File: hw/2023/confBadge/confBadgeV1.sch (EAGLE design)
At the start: 51 parts, among them J1 10118192-0002LF, Q1 8/16/20MHz, U1 ATMEGA328, U10 WS2812-2020, U11 WS2812-2020, U12 WS2812-2020, U13 WS2812-2020, U14 WS2812-2020, U15 WS2812-2020, U16 WS2812-2020, U17 WS2812-2020, U18 WS2812-2020, U19 WS2812-2020, U2 AP2112-3.3, U20 WS2812-2020, U3 WS2812-2020, U4 WS2812-2020, U5 PCM12SMTRPCM12SMTR_CNK, U6 24792479PCB_37P49X52P63_KEY, U7 CH340C, U8 SMF05CT1G, U9 WS2812-2020

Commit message: Completed part placement
- parts placement done
-added cap to each neopixel
- connected usb power to regulator
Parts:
- added C10, C11, C12, C13, C14, C15, C16, C17, C18, C19, C4, C5, C6, C7, C8, C9: 0.1uF, SparkFun:CAP0603-CAP
- added D2: RED, microbuilder:LED0805_NOOUTLINE
- added U21, U22: WS2812-2020, WS2812-2020:WS2812-2020
- D3: value Green -> MBR120; device Testing:LED -> microbuilder:DIODE-SCHOTTKYSOD-123
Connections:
- removed net VCC: C3.2
- new net N$17: U20.DO, U21.DI
- new net N$20: U21.DO, U22.DI
- net 3.3V: now also C3.2
- net GND: now also C10.1, C11.1, C12.1, C13.1, C14.1, C15.1, C16.1, C17.1, C18.1, C19.1, C4.1, C5.1, C6.1, C7.1, C8.1, C9.1, D2.C, U21.GND, U22.GND; no longer D3.C
- net N$34: now also D3.C
- net N$7: now also D2.A; no longer D3.A
- net VBUS: now also D3.A
- net VDD: now also C10.2, C11.2, C12.2, C13.2, C14.2, C15.2, C16.2, C17.2, C18.2, C19.2, C4.2, C5.2, C6.2, C7.2, C8.2, C9.2, U21.VDD, U22.VDD
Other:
- moved on the sheet: U10, U11, U12, U13, U14, U15, U16, U17, U18, U19, U20, U3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

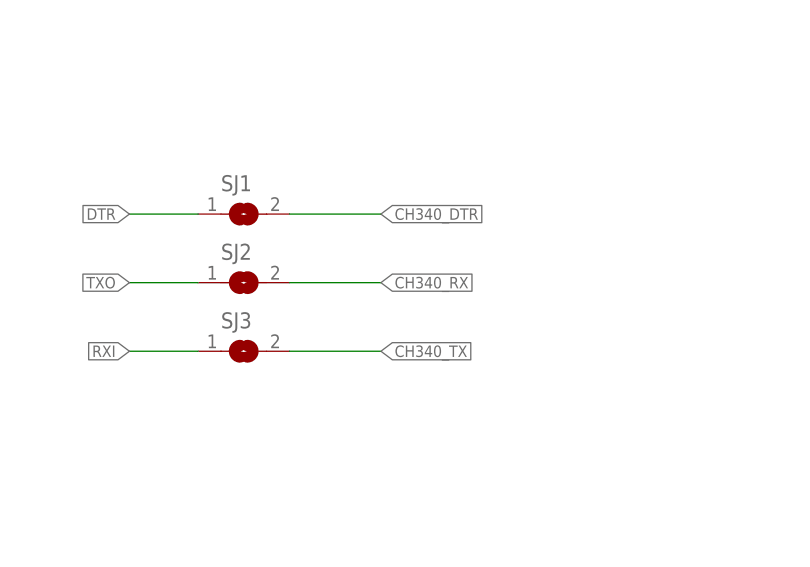
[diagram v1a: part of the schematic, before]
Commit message: Tested monochrome bitmap
Added Rao to the back of the confBadge for testing
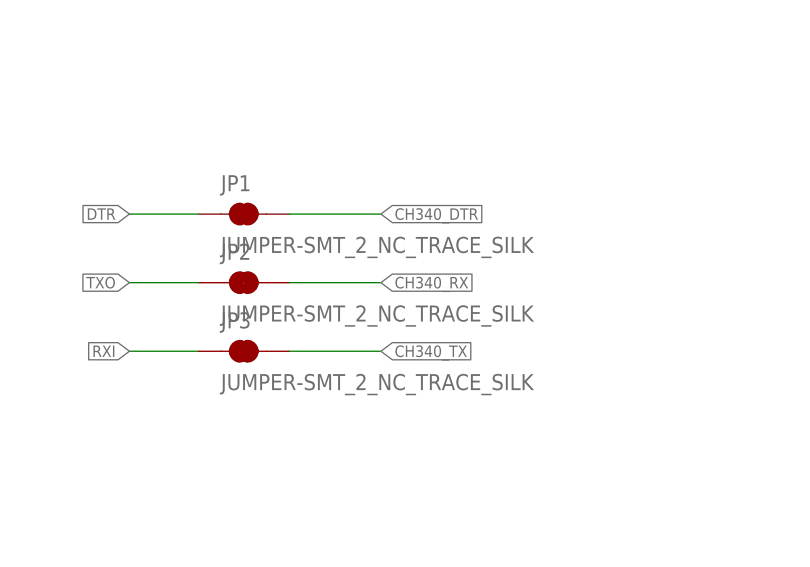
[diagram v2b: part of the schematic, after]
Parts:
- removed SJ1, SJ2, SJ3: (no value), jumper:SJ
- added JP1, JP2, JP3: JUMPER-SMT_2_NC_TRACE_SILK, SparkFun-Jumpers:JUMPER-SMT_2_NC_TRACE_SILK
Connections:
- net CH340_DTR: now also JP1.2; no longer SJ1.2
- net CH340_RX: now also JP2.2; no longer SJ2.2
- net CH340_TX: now also JP3.2; no longer SJ3.2
- net DTR: now also JP1.1; no longer SJ1.1
- net RXI: now also JP3.1; no longer SJ3.1
- net TXO: now also JP2.1; no longer SJ2.1
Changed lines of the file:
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@@
 <part name="U$6" library="microbuilder" deviceset="GND" device=""/>
 <part name="U$7" library="microbuilder" deviceset="VBUS" device=""/>
-<part name="SJ1" library="jumper" library_urn="urn:adsk.eagle:library:252" deviceset="SJ" device="" package3d_urn="urn:adsk.eagle:package:15471/1"/>
-<part name="SJ2" library="jumper" library_urn="urn:adsk.eagle:library:252" deviceset="SJ" device="" package3d_urn="urn:adsk.eagle:package:15471/1"/>
-<part name="SJ3" library="jumper" library_urn="urn:adsk.eagle:library:252" deviceset="SJ" device="" package3d_urn="urn:adsk.eagle:package:15471/1"/>
 <part name="U$3" library="microbuilder" deviceset="3.3V" device=""/>
 <part name="U$4" library="microbuilder" deviceset="3.3V" device=""/>
@@
 <part name="D3" library="microbuilder" deviceset="DIODE-SCHOTTKY" device="SOD-123" value="MBR120"/>
 <part name="U$40" library="microbuilder" deviceset="VBUS" device=""/>
+<part name="JP1" library="SparkFun-Jumpers" deviceset="JUMPER-SMT_2_NC_TRACE" device="_SILK" package3d_urn="urn:adsk.eagle:package:39281/1"/>
+<part name="JP2" library="SparkFun-Jumpers" deviceset="JUMPER-SMT_2_NC_TRACE" device="_SILK" package3d_urn="urn:adsk.eagle:package:39281/1"/>
+<part name="JP3" library="SparkFun-Jumpers" deviceset="JUMPER-SMT_2_NC_TRACE" device="_SILK" package3d_urn="urn:adsk.eagle:package:39281/1"/>
 </parts>
 <sheets>
@@
 <attribute name="VALUE" x="445.516" y="140.716" size="1.27" layer="96"/>
 </instance>
-<instance part="SJ1" gate="1" x="220.98" y="154.94" smashed="yes">
-<attribute name="NAME" x="218.44" y="157.48" size="1.778" layer="95"/>
-<attribute name="VALUE" x="218.44" y="151.13" size="1.778" layer="96"/>
-</instance>
-<instance part="SJ2" gate="1" x="220.98" y="147.32" smashed="yes">
-<attribute name="NAME" x="218.44" y="149.86" size="1.778" layer="95"/>
-<attribute name="VALUE" x="218.44" y="143.51" size="1.778" layer="96"/>
-</instance>
-<instance part="SJ3" gate="1" x="220.98" y="139.7" smashed="yes">
-<attribute name="NAME" x="218.44" y="142.24" size="1.778" layer="95"/>
-<attribute name="VALUE" x="218.44" y="135.89" size="1.778" layer="96"/>
-</instance>
 <instance part="U$3" gate="G$1" x="96.52" y="116.84" smashed="yes">
 <attribute name="VALUE" x="94.996" y="117.856" size="1.27" layer="96"/>
@@
 <instance part="U$40" gate="G$1" x="86.36" y="284.48" smashed="yes">
 <attribute name="VALUE" x="84.836" y="285.496" size="1.27" layer="96"/>
+</instance>
+<instance part="JP1" gate="G$1" x="220.98" y="154.94" smashed="yes">
+<attribute name="NAME" x="218.44" y="157.48" size="1.778" layer="95" font="vector"/>
+<attribute name="VALUE" x="218.44" y="152.4" size="1.778" layer="96" font="vector" align="top-left"/>
+</instance>
+<instance part="JP2" gate="G$1" x="220.98" y="147.32" smashed="yes">
+<attribute name="NAME" x="218.44" y="149.86" size="1.778" layer="95" font="vector"/>
+<attribute name="VALUE" x="218.44" y="144.78" size="1.778" layer="96" font="vector" align="top-left"/>
+</instance>
+<instance part="JP3" gate="G$1" x="220.98" y="139.7" smashed="yes">
+<attribute name="NAME" x="218.44" y="142.24" size="1.778" layer="95" font="vector"/>
+<attribute name="VALUE" x="218.44" y="137.16" size="1.778" layer="96" font="vector" align="top-left"/>
 </instance>
 </instances>
@@
 <segment>
 <label x="208.28" y="147.32" size="1.27" layer="95" rot="R180" xref="yes"/>
-<pinref part="SJ2" gate="1" pin="1"/>
 <wire x1="208.28" y1="147.32" x2="215.9" y2="147.32" width="0.1524" layer="91"/>
+<pinref part="JP2" gate="G$1" pin="1"/>
 </segment>
 </net>
@@
 <wire x1="215.9" y1="154.94" x2="208.28" y2="154.94" width="0.1524" layer="91"/>
 <label x="208.28" y="154.94" size="1.27" layer="95" rot="R180" xref="yes"/>
-<pinref part="SJ1" gate="1" pin="1"/>
+<pinref part="JP1" gate="G$1" pin="1"/>
 </segment>
 </net>
@@
 <segment>
 <label x="208.28" y="139.7" size="1.27" layer="95" rot="R180" xref="yes"/>
-<pinref part="SJ3" gate="1" pin="1"/>
 <wire x1="208.28" y1="139.7" x2="215.9" y2="139.7" width="0.1524" layer="91"/>
+<pinref part="JP3" gate="G$1" pin="1"/>
 </segment>
 </net>
@@
 <segment>
 <wire x1="226.06" y1="154.94" x2="236.22" y2="154.94" width="0.1524" layer="91"/>
-<pinref part="SJ1" gate="1" pin="2"/>
 <label x="236.22" y="154.94" size="1.27" layer="95" xref="yes"/>
+<pinref part="JP1" gate="G$1" pin="2"/>
 </segment>
 </net>
@@
 <segment>
 <wire x1="226.06" y1="139.7" x2="236.22" y2="139.7" width="0.1524" layer="91"/>
-<pinref part="SJ3" gate="1" pin="2"/>
 <label x="236.22" y="139.7" size="1.27" layer="95" xref="yes"/>
+<pinref part="JP3" gate="G$1" pin="2"/>
 </segment>
 </net>
@@
 <segment>
 <wire x1="236.22" y1="147.32" x2="226.06" y2="147.32" width="0.1524" layer="91"/>
-<pinref part="SJ2" gate="1" pin="2"/>
 <label x="236.22" y="147.32" size="1.27" layer="95" xref="yes"/>
-</segment>
-</net>
+<pinref part="JP2" gate="G$1" pin="2"/>
+</segment>
+</net>

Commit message: finished routing layout
- added soldering village track
(1) through-hole + smd led at the top
(2) oled
(3) 2 button at the bottom right
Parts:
- added D6, D7: NC, microbuilder:LED0805_NOOUTLINE
- added LED2, LED3: NC, led:LED3MM
- added LED7, LED8: NC, led:LEDCHIPLED_1206
- added R10, R11: NC, rcl:R-US_R1206W
- added R12, R15: NC, microbuilder:RESISTOR_0603_NOOUT
- added R3, R4: NC, rcl:R-US_0207/10
- added SV4: SAO, con-lstb:MA03-2
- S1: value (none) -> RST
- S2, S3: value (none) -> NC
- S4: value (none) -> U
- S5: value (none) -> D
- S6: value (none) -> L
- S7: value (none) -> R
- SV1: value (none) -> SYNCOUT
- SV2: value (none) -> SYNCIN
- SV3: value (none) -> OLED
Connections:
- removed net BTN4: U1.PC3(ADC3)
- removed net BTNB: U1.ADC6
- removed net D7: SV1.3
- new net N$18: D6.A, R12.2
- new net N$19: LED2.A, R3.2
- new net N$21: LED3.A, R4.2
- new net N$22: D7.A, R15.2
- new net N$25: LED8.A, R10.1
- new net N$26: LED7.A, R11.1
- new net SAO_IO1: SV4.6, U1.PB3(MOSI/OC2)
- new net SAO_IO2: SV4.5, U1.PB4(MISO)
- net 3.3V: now also R10.2, R11.2, R12.1, R15.1, R3.1, R4.1, SV4.2
- net BTN_B: now also U1.ADC6
- net BTN_L: now also U1.PC3(ADC3)
- net GND: now also D6.C, D7.C, LED2.C, LED3.C, LED7.C, LED8.C, SV4.1
- net SCL: now also SV4.3
- net SDA: now also SV4.4
- net SIG_OUT3: now also SV1.3
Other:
- note added: "SOLDERING VILLAGE LEDS"
- note added: "SOLDERING VILLAGE OLED (0.91in OLED Module White/Blue 128X32)"
- note removed: "optional oled screen / soldering village 0.91in OLED Module White/Blue 128X32"
- moved on the sheet: SV3

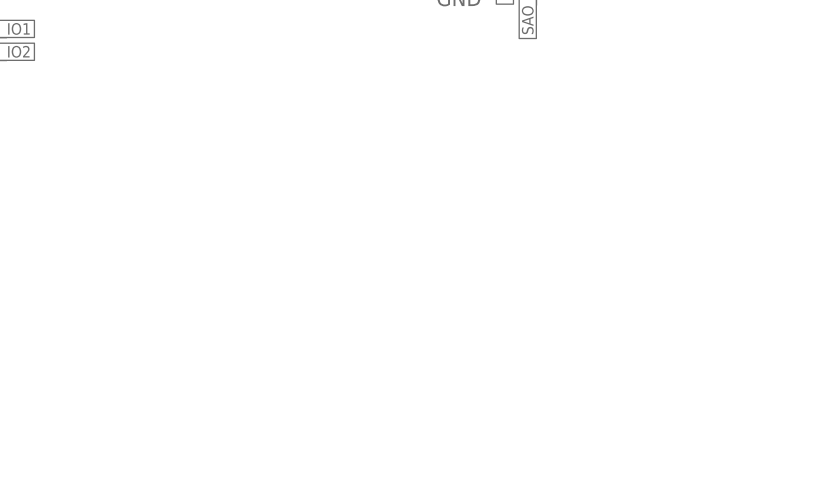
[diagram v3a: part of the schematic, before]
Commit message: Added ISP header
ISP header added for programming bootloader
and adjusted top silkscreen to show footprint for soldering village activity
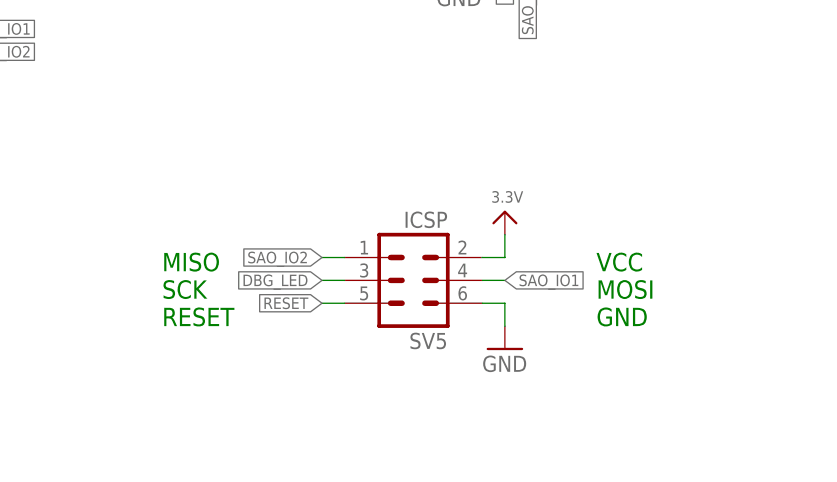
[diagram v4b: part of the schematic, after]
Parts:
- added SV5: ICSP, con-lstb:MA03-2
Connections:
- net 3.3V: now also SV5.2
- net DBG_LED: now also SV5.3
- net GND: now also SV5.6
- net RESET: now also SV5.5
- net SAO_IO1: now also SV5.4
- net SAO_IO2: now also SV5.1
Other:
- note added: "MISO SCK RESET"
- note added: "VCC MOSI GND"
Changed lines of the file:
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@@
 <part name="FRAME6" library="frames" library_urn="urn:adsk.eagle:library:229" deviceset="A4L-LOC" device="" value="SOLDERING"/>
 <part name="FRAME7" library="frames" library_urn="urn:adsk.eagle:library:229" deviceset="A4L-LOC" device="" value="USB"/>
+<part name="SV5" library="con-lstb" library_urn="urn:adsk.eagle:library:162" deviceset="MA03-2" device="" package3d_urn="urn:adsk.eagle:package:8334/1" value="ICSP"/>
+<part name="GND11" library="SparkFun" deviceset="GND" device=""/>
+<part name="U$48" library="microbuilder" deviceset="3.3V" device=""/>
 </parts>
 <sheets>
@@
 <wire x1="703.58" y1="114.3" x2="708.66" y2="119.38" width="0.1524" layer="97"/>
 <wire x1="708.66" y1="119.38" x2="708.66" y2="149.86" width="0.1524" layer="97"/>
+<text x="195.58" y="35.56" size="2.032" layer="91">MISO
+SCK
+RESET</text>
+<text x="243.84" y="35.56" size="2.032" layer="91">VCC
+MOSI
+GND</text>
 </plain>
 <instances>
@@
 <attribute name="LAST_DATE_TIME" x="483.87" y="10.16" size="2.286" layer="94"/>
 <attribute name="SHEET" x="497.205" y="5.08" size="2.54" layer="94"/>
+</instance>
+<instance part="SV5" gate="1" x="223.52" y="40.64" smashed="yes" rot="R180">
+<attribute name="VALUE" x="227.33" y="48.26" size="1.778" layer="96" rot="R180"/>
+<attribute name="NAME" x="227.33" y="34.798" size="1.778" layer="95" rot="R180"/>
+</instance>
+<instance part="GND11" gate="1" x="233.68" y="33.02" smashed="yes">
+<attribute name="VALUE" x="231.14" y="30.48" size="1.778" layer="96"/>
+</instance>
+<instance part="U$48" gate="G$1" x="233.68" y="48.26" smashed="yes">
+<attribute name="VALUE" x="232.156" y="49.276" size="1.27" layer="96"/>
 </instance>
 </instances>
@@
 <junction x="675.64" y="132.08"/>
 </segment>
+<segment>
+<pinref part="SV5" gate="1" pin="6"/>
+<wire x1="231.14" y1="38.1" x2="233.68" y2="38.1" width="0.1524" layer="91"/>
+<pinref part="GND11" gate="1" pin="GND"/>
+<wire x1="233.68" y1="38.1" x2="233.68" y2="35.56" width="0.1524" layer="91"/>
+</segment>
 </net>
 <net name="AREF" class="0">
@@
 <pinref part="S1" gate="G$1" pin="4"/>
 </segment>
+<segment>
+<wire x1="215.9" y1="38.1" x2="213.36" y2="38.1" width="0.1524" layer="91"/>
+<pinref part="SV5" gate="1" pin="5"/>
+<label x="213.36" y="38.1" size="1.27" layer="95" rot="R180" xref="yes"/>
+</segment>
 </net>
 <net name="DBG_LED" class="0">
@@
 <wire x1="157.48" y1="63.5" x2="160.02" y2="63.5" width="0.1524" layer="91"/>
 <label x="160.02" y="63.5" size="1.27" layer="95" xref="yes"/>
+</segment>
+<segment>
+<wire x1="213.36" y1="40.64" x2="215.9" y2="40.64" width="0.1524" layer="91"/>
+<pinref part="SV5" gate="1" pin="3"/>
+<label x="213.36" y="40.64" size="1.27" layer="95" rot="R180" xref="yes"/>
 </segment>
 </net>
@@
 <wire x1="627.38" y1="139.7" x2="627.38" y2="142.24" width="0.1524" layer="91"/>
 <junction x="627.38" y="139.7"/>
+</segment>
+<segment>
+<pinref part="SV5" gate="1" pin="2"/>
+<wire x1="231.14" y1="43.18" x2="233.68" y2="43.18" width="0.1524" layer="91"/>
+<pinref part="U$48" gate="G$1" pin="3.3V"/>
+<wire x1="233.68" y1="43.18" x2="233.68" y2="45.72" width="0.1524" layer="91"/>
 </segment>
 </net>
@@
 <label x="236.22" y="101.6" size="1.27" layer="95" rot="R90" xref="yes"/>
 </segment>
+<segment>
+<wire x1="231.14" y1="40.64" x2="233.68" y2="40.64" width="0.1524" layer="91"/>
+<pinref part="SV5" gate="1" pin="4"/>
+<label x="233.68" y="40.64" size="1.27" layer="95" xref="yes"/>
+</segment>
 </net>
 <net name="SAO_IO2" class="0">
@@
 <label x="236.22" y="76.2" size="1.27" layer="95" rot="R270" xref="yes"/>
 </segment>
-</net>
+<segment>
+<wire x1="213.36" y1="43.18" x2="215.9" y2="43.18" width="0.1524" layer="91"/>
+<pinref part="SV5" gate="1" pin="1"/>
+<label x="213.36" y="43.18" size="1.27" layer="95" rot="R180" xref="yes"/>
+</segment>
+</net>

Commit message: Created gerbers
- changed some footprint to only have 0.1uF at 0603 (removed 0805)
- created gerbers and pick-n-place files for JLCPCB
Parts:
- removed C25: 1uF, microbuilder:CAP_CERAMIC0805-NOOUTLINE
- removed C29: 0.1uF, microbuilder:CAP_CERAMIC0805-NOOUTLINE
- added C20: 0.1uF, SparkFun:CAP0603-CAP
- added C21: 1uF, microbuilder:CAP_CERAMIC0603_NO
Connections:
- net 3.3V: now also C20.2; no longer C29.1
- net GND: now also C20.1, C21.2; no longer C25.2, C29.2
- net VDD: now also C21.1; no longer C25.1
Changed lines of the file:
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@@
 <part name="C2" library="SparkFun" deviceset="CAP" device="0603-CAP" value="0.1uF"/>
 <part name="Q1" library="Testing" deviceset="RESONATOR" device="1:1" value="8/16/20MHz"/>
-<part name="C25" library="microbuilder" deviceset="CAP_CERAMIC" device="0805-NOOUTLINE" value="1uF"/>
 <part name="C26" library="microbuilder" deviceset="CAP_CERAMIC" device="0603_NO" value="1uF"/>
 <part name="U$27" library="microbuilder" deviceset="GND" device=""/>
@@
 <part name="FRAME4" library="frames" library_urn="urn:adsk.eagle:library:229" deviceset="A4L-LOC" device="" value="BUTTON"/>
 <part name="U$11" library="microbuilder" deviceset="GND" device=""/>
-<part name="C29" library="microbuilder" deviceset="CAP_CERAMIC" device="0805-NOOUTLINE" value="0.1uF"/>
 <part name="U$17" library="microbuilder" deviceset="GND" device=""/>
 <part name="U$18" library="microbuilder" deviceset="VBUS" device=""/>
@@
 <part name="GND11" library="SparkFun" deviceset="GND" device=""/>
 <part name="U$48" library="microbuilder" deviceset="3.3V" device=""/>
+<part name="C20" library="SparkFun" deviceset="CAP" device="0603-CAP" value="0.1uF"/>
+<part name="C21" library="microbuilder" deviceset="CAP_CERAMIC" device="0603_NO" value="1uF"/>
 </parts>
 <sheets>
@@
 <attribute name="VALUE" x="97.282" y="88.392" size="1.778" layer="96"/>
 </instance>
-<instance part="C25" gate="G$1" x="172.72" y="276.86" smashed="yes">
-<attribute name="NAME" x="170.43" y="278.11" size="1.27" layer="95" font="vector" rot="R90" align="center"/>
-<attribute name="VALUE" x="175.02" y="278.11" size="1.27" layer="96" font="vector" rot="R90" align="center"/>
-</instance>
 <instance part="C26" gate="G$1" x="228.6" y="276.86" smashed="yes">
 <attribute name="NAME" x="226.31" y="278.11" size="1.27" layer="95" font="vector" rot="R90" align="center"/>
@@
 <attribute name="VALUE" x="364.236" y="139.7" size="1.27" layer="96"/>
 </instance>
-<instance part="C29" gate="G$1" x="406.4" y="78.74" smashed="yes">
-<attribute name="NAME" x="404.11" y="79.99" size="1.27" layer="95" font="vector" rot="R90" align="center"/>
-<attribute name="VALUE" x="408.7" y="79.99" size="1.27" layer="96" font="vector" rot="R90" align="center"/>
-</instance>
 <instance part="U$17" gate="G$1" x="406.4" y="71.12" smashed="yes">
 <attribute name="VALUE" x="404.876" y="68.58" size="1.27" layer="96"/>
@@
 <instance part="U$48" gate="G$1" x="233.68" y="48.26" smashed="yes">
 <attribute name="VALUE" x="232.156" y="49.276" size="1.27" layer="96"/>
+</instance>
+<instance part="C20" gate="G$1" x="406.4" y="81.28" smashed="yes" rot="R180">
+<attribute name="NAME" x="407.416" y="81.407" size="1.778" layer="95"/>
+<attribute name="VALUE" x="407.416" y="76.581" size="1.778" layer="96"/>
+</instance>
+<instance part="C21" gate="G$1" x="172.72" y="276.86" smashed="yes">
+<attribute name="NAME" x="170.43" y="278.11" size="1.27" layer="95" font="vector" rot="R90" align="center"/>
+<attribute name="VALUE" x="175.02" y="278.11" size="1.27" layer="96" font="vector" rot="R90" align="center"/>
 </instance>
 </instances>
@@
 </segment>
 <segment>
-<pinref part="C25" gate="G$1" pin="2"/>
 <pinref part="U$27" gate="G$1" pin="GND"/>
 <wire x1="172.72" y1="274.32" x2="172.72" y2="271.78" width="0.1524" layer="91"/>
+<pinref part="C21" gate="G$1" pin="2"/>
 </segment>
 <segment>
@@
 </segment>
 <segment>
-<pinref part="C29" gate="G$1" pin="2"/>
 <pinref part="U$17" gate="G$1" pin="GND"/>
 <wire x1="406.4" y1="76.2" x2="406.4" y2="73.66" width="0.1524" layer="91"/>
+<pinref part="C20" gate="G$1" pin="1"/>
 </segment>
 <segment>
@@
 </segment>
 <segment>
-<pinref part="C29" gate="G$1" pin="1"/>
 <wire x1="406.4" y1="83.82" x2="406.4" y2="86.36" width="0.1524" layer="91"/>
 <pinref part="U$24" gate="G$1" pin="3.3V"/>
@@
 <wire x1="401.32" y1="73.66" x2="401.32" y2="76.2" width="0.1524" layer="91"/>
 <junction x="401.32" y="76.2"/>
+<pinref part="C20" gate="G$1" pin="2"/>
 </segment>
 <segment>
@@
 <net name="VDD" class="0">
 <segment>
-<pinref part="C25" gate="G$1" pin="1"/>
 <wire x1="182.88" y1="287.02" x2="172.72" y2="287.02" width="0.1524" layer="91"/>
 <wire x1="172.72" y1="287.02" x2="172.72" y2="281.94" width="0.1524" layer="91"/>
@@
 <wire x1="162.56" y1="284.48" x2="162.56" y2="287.02" width="0.1524" layer="91"/>
 <junction x="162.56" y="287.02"/>
-</segment>
-<segment>
+<pinref part="C21" gate="G$1" pin="1"/>
+</segment>
+<segment>

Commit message: Switch to USB-C for both badge
ctf-badge
- switched to USB-C
- switched to smaller neopixel
- switched to 3xAAA
- removed lipo charging circuit
conf-badge
- switched to USB-C
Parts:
- removed J1: 10118192-0002LF, 10118192-0002LF:10118192-0002LF
- added J3: TYPE-C-31-M-12, TYPE-C-31-M-12:TYPE-C-31-M-12
- added R1, R5: 5.1K, microbuilder:RESISTOR_0603_NOOUT
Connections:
- removed net N$28: J1.D+, U7.UD+, U8.C4
- removed net N$29: J1.D-, U7.UD-, U8.C5
- new net N$27: J3.CC2, R5.1
- new net N$30: J3.CC1, R1.1
- new net USB_DN: J3.DN1, J3.DN2, U7.UD-, U8.C5
- new net USB_DP: J3.DP1, J3.DP2, U7.UD+, U8.C4
- net GND: now also J3.GND, J3.SHIELD, R1.2, R5.2; no longer J1.GND, J1.SHIELD
- net VBUS: now also J3.VBUS; no longer J1.VCC
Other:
- note added: "Mnfr: Korean Hroparts Elec Part#: TYPE-C-31-M-14 JLCPCB#: C223907"
